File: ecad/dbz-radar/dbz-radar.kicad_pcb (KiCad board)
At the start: 2 copper layers, 139 parts, among them J1 B2B-PH-SM4-TB, J2 USB4220-03-0880-C, J3 XF2M-4015-1A, J4 533980271, Q1 Q_PMOS, SW1 SW_Push, SW2 SW_Push, U1 USBLC6-2SC6, U2 TPS61169, U3 MCP738311/2, U4 MAX17048/9, U5 AP2112K-3.3, U6 PCA9554, U7 MAX98357A, U8 ESP32-S3-WROOM-1

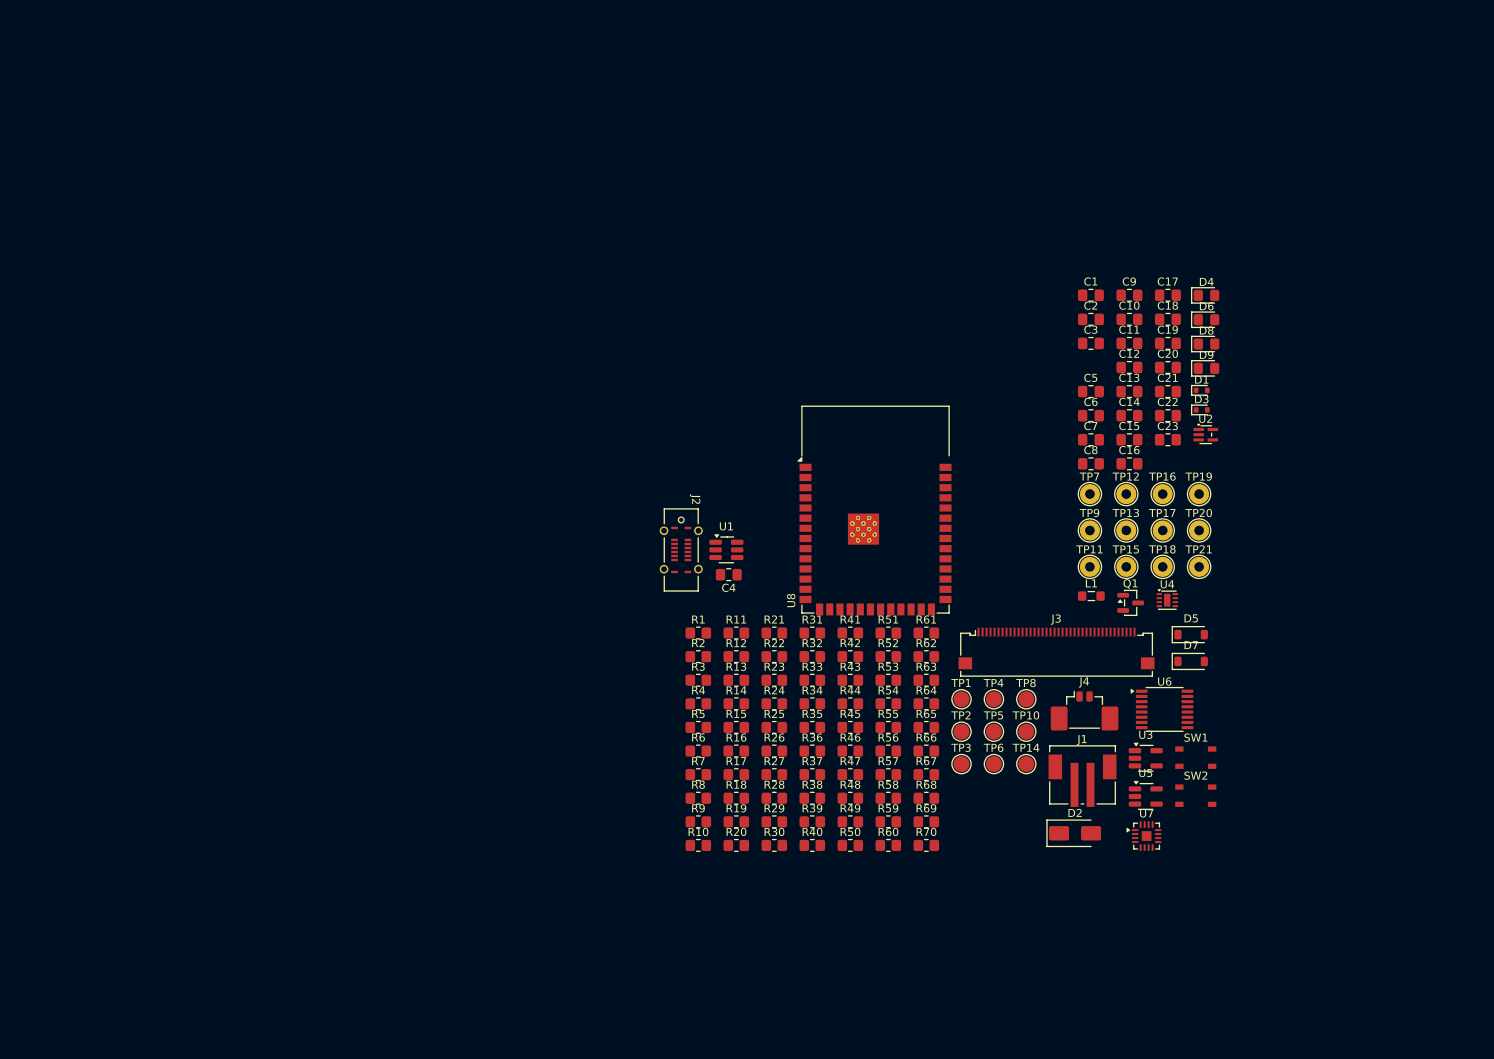
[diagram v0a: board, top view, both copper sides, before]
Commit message: add user button symbol and footprints to layout
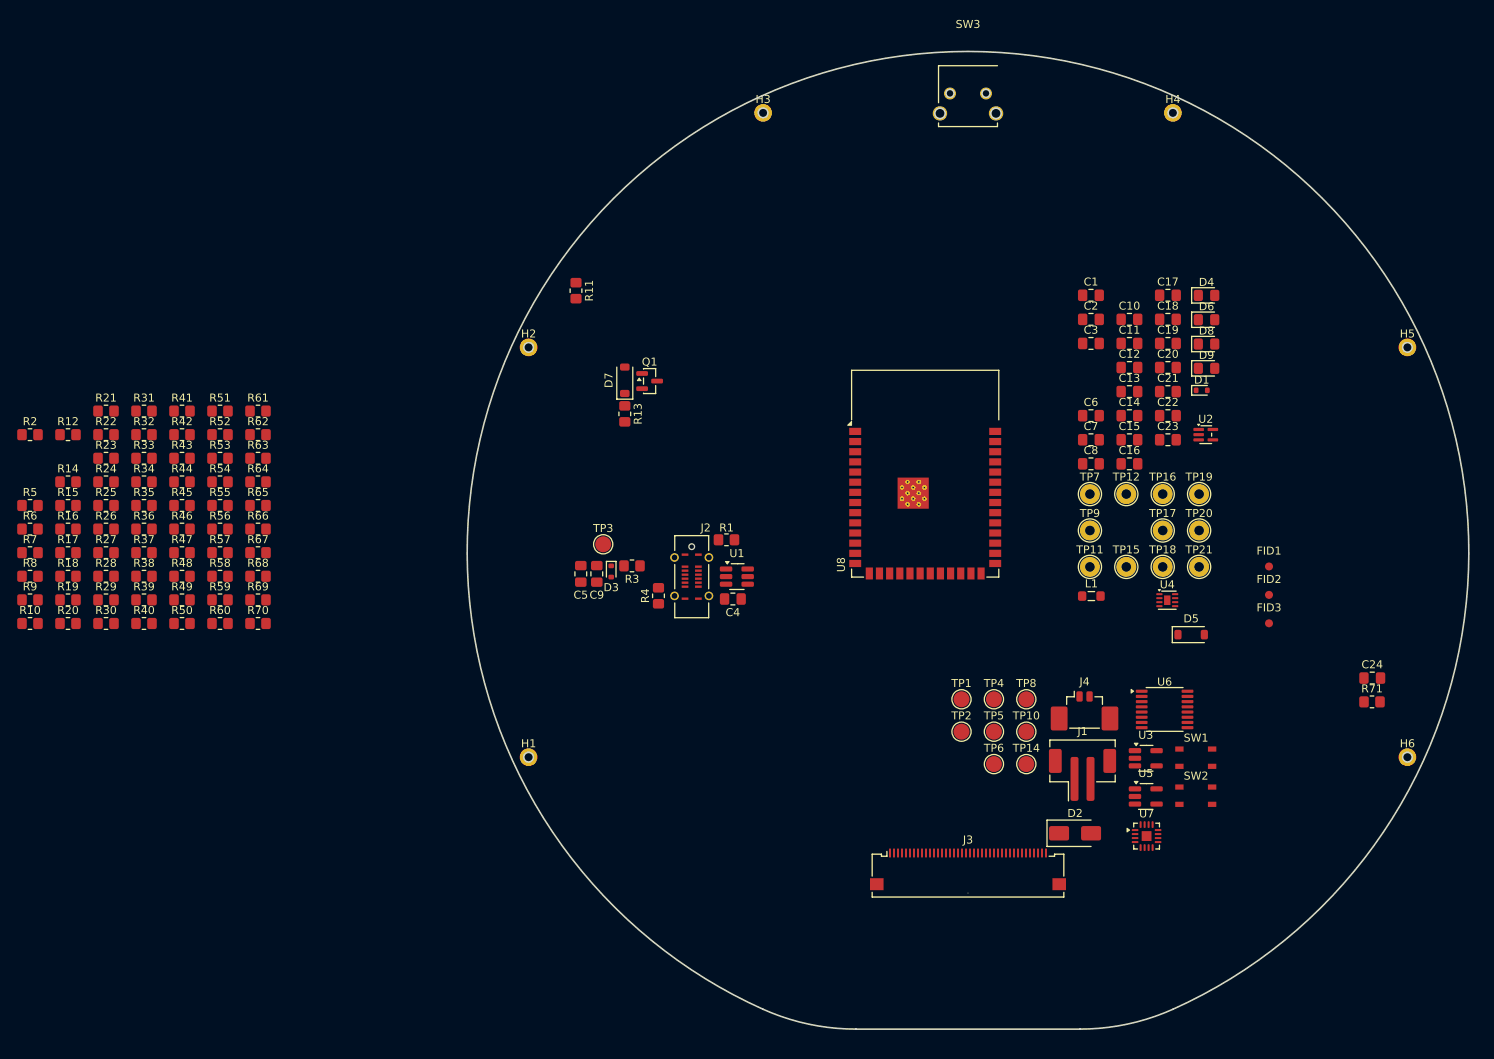
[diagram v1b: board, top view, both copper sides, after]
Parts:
- removed TP13: TestPoint_Alt, TestPoint:TestPoint_THTPad_D2.5mm_Drill1.2mm
- added C24: 100nF, Capacitor_SMD:C_0805_2012Metric_Pad1.18x1.45mm_HandSolder, F.Cu at (190.1, 109.5)
- added FID1: Fiducial, Fiducial:Fiducial_1mm_Mask2mm, F.Cu at (177.2, 95.6)
- added FID2: Fiducial, Fiducial:Fiducial_1mm_Mask2mm, F.Cu at (177.2, 99.1)
- added FID3: Fiducial, Fiducial:Fiducial_1mm_Mask2mm, F.Cu at (177.2, 102.7)
- added H1: MountingHole_Pad, M1:M1-mounting-hole, F.Cu at (84.7, 119.4)
- added H2: MountingHole_Pad, M1:M1-mounting-hole, F.Cu at (84.7, 68.2)
- added H3: MountingHole_Pad, M1:M1-mounting-hole, F.Cu at (114.0, 38.9)
- added H4: MountingHole_Pad, M1:M1-mounting-hole, F.Cu at (165.2, 38.9)
- added H5: MountingHole_Pad, M1:M1-mounting-hole, F.Cu at (194.5, 68.2)
- added H6: MountingHole_Pad, M1:M1-mounting-hole, F.Cu at (194.5, 119.4)
- added R71: 5.1k, Resistor_SMD:R_0805_2012Metric_Pad1.20x1.40mm_HandSolder, F.Cu at (190.1, 112.5)
- added SW3: 1-825027-7, 1-825027-7:1-825027-7, F.Cu at (139.6, 37.7)
- J1: footprint B2B-PH-SM4-TBLFSN_JST:B2B-PH-SM4-TB -> B2B-PH-SM4-TB:B2B-PH-SM4-TB
- J3: footprint Connector_FFC-FPC:Omron_XF2M-4015-1A_1x40-1MP_P0.5mm_Horizontal -> XF2M-4015-1A:XF2M-4015-1A
- SW1, SW2: value SW_Push -> SKRPACE010
- U4: footprint Package_DFN_QFN:DFN-8-1EP_2x2mm_P0.5mm_EP0.8x1.6mm -> MAX1704X:MAX1704X
- U7: footprint Package_DFN_QFN:TQFN-16-1EP_3x3mm_P0.5mm_EP1.23x1.23mm -> MAX98357XTEXX:MAX98357XTEXX
- moved R10 88.0 mm to (22.4, 102.7)
- moved R12 88.0 mm to (27.1, 79.1)
- moved R14 88.0 mm to (27.1, 85.0)
- moved R15 88.0 mm to (27.1, 88.0)
- moved R16 88.0 mm to (27.1, 90.9)
- moved R17 88.0 mm to (27.1, 93.8)
- moved R18 88.0 mm to (27.1, 96.8)
- moved R19 88.0 mm to (27.1, 99.8)
- moved R2 88.0 mm to (22.4, 79.1)
- moved R20 88.0 mm to (27.1, 102.7)
- moved R21 88.0 mm to (31.9, 76.2)
- moved R22 88.0 mm to (31.9, 79.1)
- moved R23 88.0 mm to (31.9, 82.0)
- moved R24 88.0 mm to (31.9, 85.0)
- moved R25 88.0 mm to (31.9, 88.0)
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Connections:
- R39 pad 1: /HB_LED -> /USER
- TP12 pad 1: Net-(U6-P5) -> Net-(U6-P6)
- U6 pad 10: Net-(U6-P5) -> /HB_LED
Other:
- board outline added: 125.2 x 122.2 mm

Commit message: part placement
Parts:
- removed TP11, TP12, TP15, TP16, TP17, TP18, TP19, TP20, TP21, TP7, TP9: TestPoint_Alt, TestPoint:TestPoint_THTPad_D2.5mm_Drill1.2mm
- added J5: Conn_01x12_Pin, Connector_PinHeader_2.54mm:PinHeader_1x12_P2.54mm_Vertical, F.Cu at (197.7, 78.9)
- added R72: 0, Resistor_SMD:R_0805_2012Metric_Pad1.20x1.40mm_HandSolder, F.Cu at (145.8, 54.6)
- J3: footprint XF2M-4015-1A:XF2M-4015-1A -> XF2M-4015-1A:XF2M-4015-1A_alt
- U8: footprint RF_Module:ESP32-S3-WROOM-1 -> ESP32-S3-WROOM-1:ESP32-S3-WROOM-1_Alt
- moved R2 159.1 mm to (171.7, 134.0), turned to 180 degrees
- moved R29 158.1 mm to (187.5, 127.9), turned to 90 degrees
- moved R33 157.6 mm to (189.6, 120.1), turned to -90 degrees
- moved R38 155.2 mm to (189.6, 71.0), turned to 135 degrees
- moved R47 151.9 mm to (191.3, 69.4), turned to 135 degrees
- moved R6 147.7 mm to (163.1, 135.7), turned to -90 degrees
- moved R23 143.0 mm to (169.1, 122.5)
- moved R22 142.8 mm to (169.1, 118.6)
- moved R24 142.7 mm to (169.1, 124.4)
- moved R37 140.8 mm to (176.4, 77.4), turned to 45 degrees
- moved R15 140.5 mm to (155.6, 144.7), turned to 180 degrees
- moved R26 140.4 mm to (169.1, 120.6), turned to 180 degrees
- moved R25 140.2 mm to (169.1, 116.7)
- moved R16 138.6 mm to (155.6, 142.8), turned to 180 degrees
- moved R28 138.4 mm to (169.1, 114.8), turned to 180 degrees
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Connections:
- net Net-(U4-QSTRT) renamed /BATT_MONITOR-QSTRT
- U6 pad 11: Net-(U6-P6) -> /I2C_IO_P6
- U8 pad 11: /SCL -> Net-(U8-IO18)
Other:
- outline, holes or cut-outs redrawn
- copper layers 2 -> 4

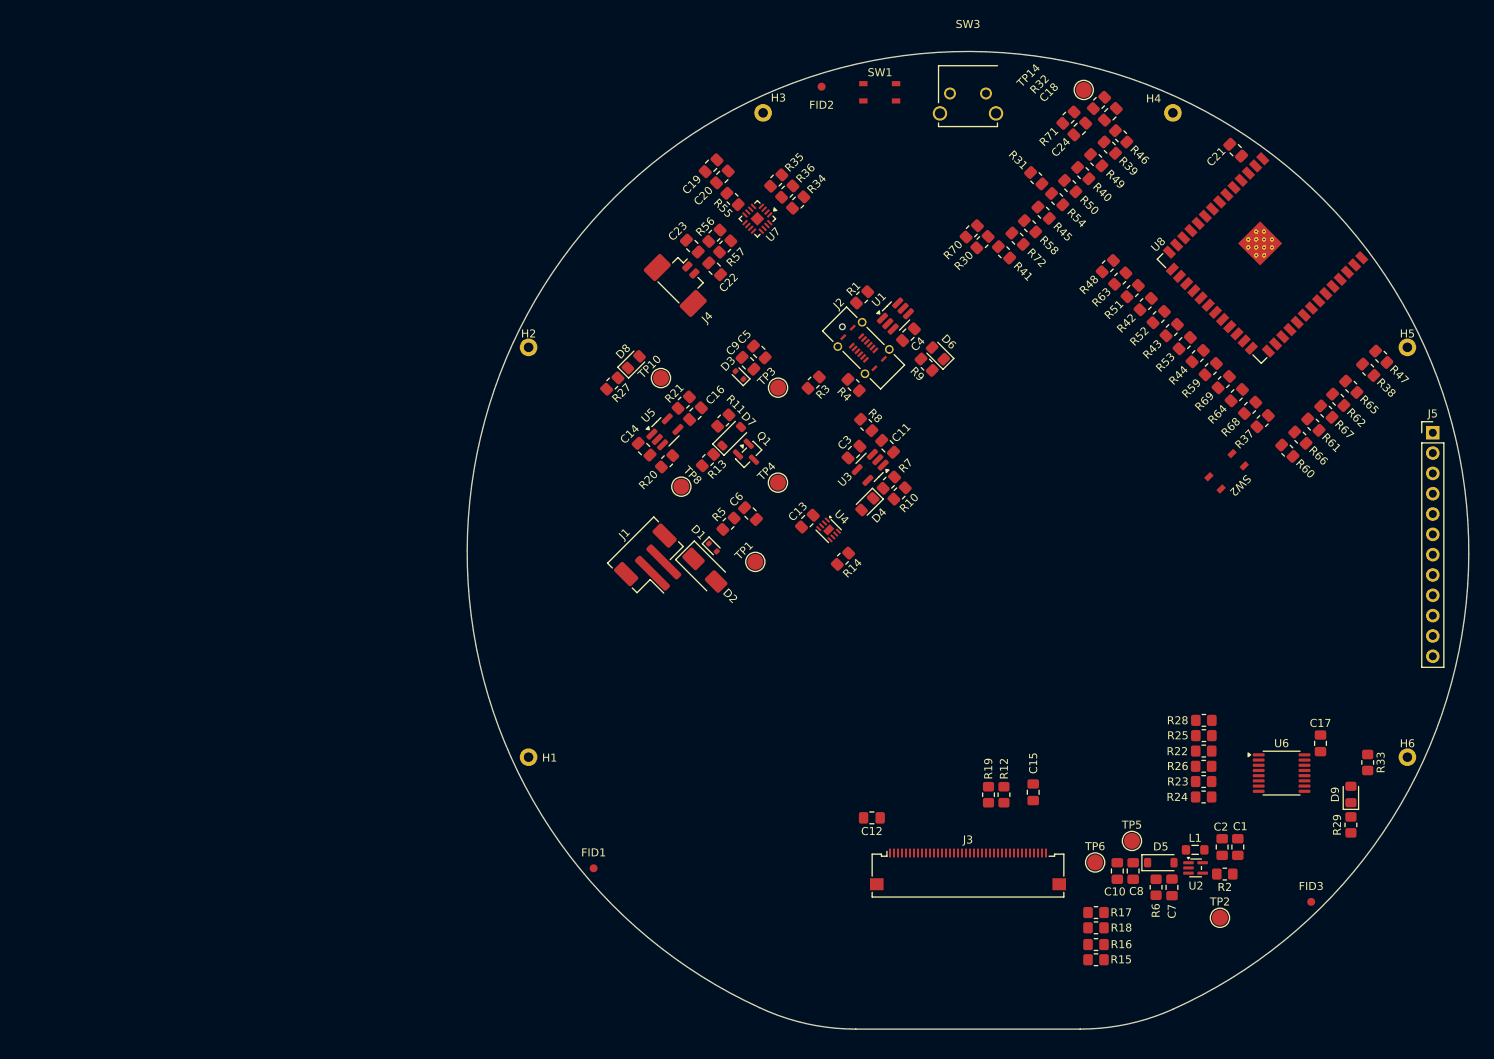
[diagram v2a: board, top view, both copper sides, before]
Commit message: start layout of power, USB
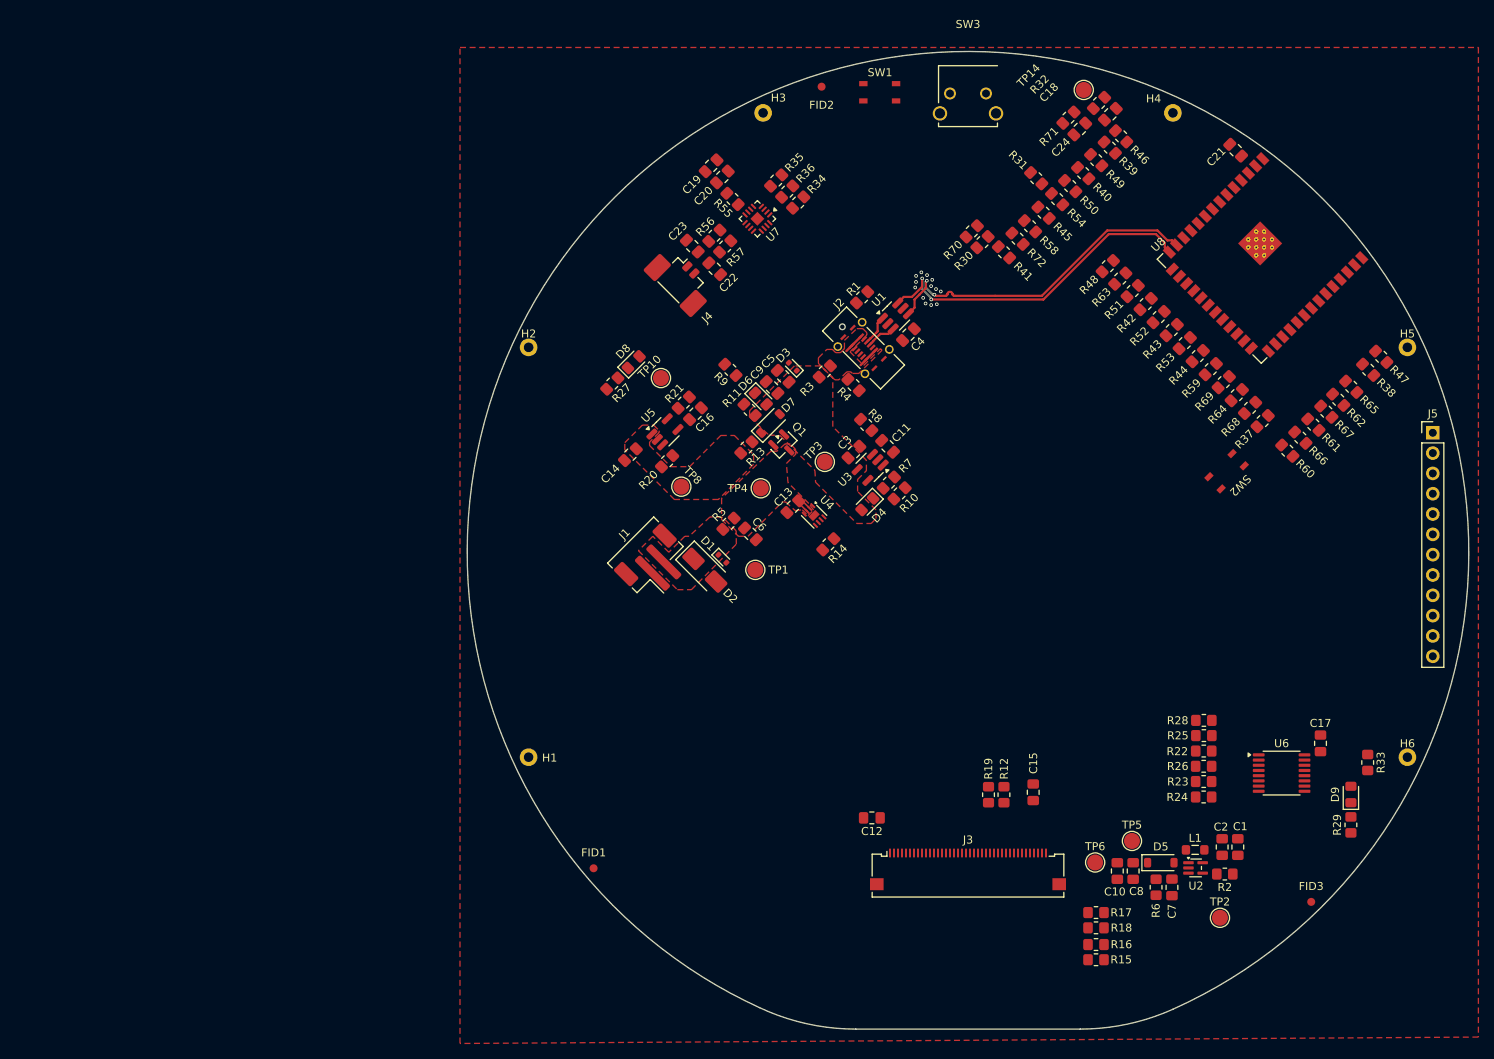
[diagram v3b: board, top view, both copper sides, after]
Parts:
- moved R9 24.5 mm to (109.9, 71.0)
- moved D6 22.9 mm to (113.7, 74.6), turned to -45 degrees
- moved TP3 11.0 mm to (121.7, 82.5)
- moved D3 6.75 mm to (117.7, 70.6)
- moved D7 5.10 mm to (114.9, 77.7)
- moved R13 5.06 mm to (111.9, 80.7)
- moved Q1 4.57 mm to (116.6, 80.4)
- moved C5 4.26 mm to (116.5, 71.8)
- moved C9 4.26 mm to (115.1, 73.2)
- moved R11 3.55 mm to (112.3, 76.0), turned to -45 degrees
- moved U4 2.56 mm to (120.4, 89.2)
- moved C13 2.56 mm to (117.7, 88.1)
- moved R14 2.56 mm to (122.1, 92.8)
- moved C6 2.54 mm to (112.4, 91.5)
- moved TP4 2.26 mm to (113.7, 85.8)
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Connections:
- net /USB_D+_CONN renamed /USB_CONN_D+
- net /USB_D-_CONN renamed /USB_CONN_D-
- net Net-(D1-K) renamed /BATT_CONN
- net Net-(J2-VBUS-PadA4) renamed /VBUS_CONN
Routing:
- net /USB_D+: track 0.00 -> 42.5 mm, vias 0 -> 2
- net /USB_D-: track 0.00 -> 42.4 mm, vias 0 -> 2
- net /VBUS_CONN: track 0.00 -> 5.22 mm
- net /USB_CONN_D+: track 0.00 -> 3.77 mm
- net /USB_CONN_D-: track 0.00 -> 3.76 mm
- net +BATT: track 0.00 -> 3.56 mm
- net GND: vias 0 -> 13
- added copper zone on F.Cu, net +BATT
- added copper zone on F.Cu, net /BATT_CONN
- added copper zone on F.Cu, net /VBUS_CONN
- added copper zone on F.Cu, net /Vin
- added copper zone on F.Cu, net GND
- added copper zone on F.Cu, net VBUS

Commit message: route USB, VBUS
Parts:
- removed C4: 100nF, Capacitor_SMD:C_0805_2012Metric_Pad1.18x1.45mm_HandSolder
- moved R4 5.64 mm to (130.7, 74.6)
- moved R1 1.52 mm to (127.5, 60.9)
- moved R3 0.30 mm to (122.0, 71.3)
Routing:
- net VBUS: track 0.00 -> 16.9 mm, vias 0 -> 2
- net /USB_CONN_D+: track 3.77 -> 13.3 mm, vias 0 -> 2
- net /USB_CONN_D-: track 3.76 -> 11.8 mm, vias 0 -> 2
- net Net-(J2-CC2): track 0.00 -> 7.10 mm, vias 0 -> 2
- net Net-(J2-CC1): track 0.00 -> 6.69 mm
- net /VBUS_CONN: track 5.22 -> 8.18 mm
- net GND: vias 13 -> 19
- net +BATT: vias 0 -> 16
- added copper zone on B.Cu, net +BATT
- added copper zone on B.Cu, net GND
- added copper zone on In1.Cu, net GND
- added copper zone on In2.Cu, net GND

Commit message: first pass layout
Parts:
- J5: footprint Connector_PinHeader_2.54mm:PinHeader_1x12_P2.54mm_Vertical -> Connector_PinHeader_2.54mm:PinHeader_1x14_P2.54mm_Vertical
- moved R16 24.5 mm to (155.0, 118.3)
- moved R15 24.5 mm to (155.0, 120.3)
- moved R18 18.5 mm to (155.0, 122.3)
- moved R17 14.7 mm to (155.0, 124.2)
- moved R28 14.6 mm to (183.2, 110.9), turned to 90 degrees
- moved R24 14.2 mm to (173.6, 110.9), turned to -90 degrees
- moved R25 13.5 mm to (181.3, 110.9), turned to -90 degrees
- moved R23 13.2 mm to (175.5, 110.9), turned to -90 degrees
- moved R29 13.2 mm to (176.1, 134.5)
- moved D9 13.2 mm to (176.1, 130.7)
- moved R22 12.9 mm to (179.3, 110.9), turned to -90 degrees
- moved R26 12.8 mm to (177.4, 110.9), turned to 90 degrees
- moved R33 9.92 mm to (185.8, 110.9)
- moved R27 8.82 mm to (93.2, 81.3)
- moved D8 8.82 mm to (95.9, 78.6)
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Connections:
- J5 pad 1: /BATT_MONITOR-QSTRT -> /TXD0
- J5 pad 10: /IO36 -> /BATT_MONITOR-QSTRT
- J5 pad 11: /IO37 -> /I2C_IO_P6
- J5 pad 12: GND -> /EXP_IRQ
- J5 pad 2: /~{BATT_ALRT} -> /SCK
- J5 pad 3: /EXP_IRQ -> /MISO
- J5 pad 4: /I2C_IO_P6 -> /MOSI
- J5 pad 5: /MOSI -> /CS
- J5 pad 6: /MISO -> /IO37
- J5 pad 7: /SCK -> /IO36
- J5 pad 8: /TXD0 -> /IO35
- J5 pad 9: /IO35 -> /~{BATT_ALRT}
- R32 pad 1: +3V3 -> /~{RESET}
- R32 pad 2: /~{RESET} -> +3V3
- SW1 pad 2: +3V3 -> /~{RESET}
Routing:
- net /SCL: track 0.00 -> 210.0 mm, vias 0 -> 4
- net /SDA: track 0.00 -> 186.6 mm, vias 0 -> 4
- net /DE: track 0.00 -> 89.7 mm
- net /RXD0: track 0.00 -> 87.9 mm, vias 0 -> 2
- net /VSYNC: track 0.00 -> 85.5 mm
- net /BATT_MONITOR-QSTRT: track 0.00 -> 82.9 mm, vias 0 -> 1
- net /HSYNC: track 0.00 -> 82.1 mm
- net /PCLK: track 0.00 -> 81.2 mm
- net /~{BATT_ALRT}: track 0.00 -> 80.4 mm, vias 0 -> 1
- net /R5: track 0.00 -> 80.0 mm
- net /B1: track 0.00 -> 79.6 mm
- net /TP_IRQ: track 0.00 -> 79.5 mm, vias 0 -> 4
- net /R4: track 0.00 -> 78.9 mm
- net /R3: track 0.00 -> 77.7 mm
- net /R1: track 0.00 -> 76.7 mm
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- added copper zone on F.Cu, net +24V
- added copper zone on B.Cu, net +3V3
- added copper zone on F.Cu, net +3V3
- added copper zone on F.Cu, net /LEDK
- added copper zone on F.Cu, net Net-(D5-A)
- added copper zone on F.Cu, net Net-(U3-Vbat)
